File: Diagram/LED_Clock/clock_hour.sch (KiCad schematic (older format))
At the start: 28 parts, among them U4 MCP23017-E_SP

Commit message: updated
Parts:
- renumbered U4 to U1
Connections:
- net at R22.2: now also U1.4 (GPB3); no longer U1.21 (GPA0)
- net at R25.2: now also U1.1 (GPB0); no longer U1.24 (GPA3)
- net at R26.2: now also U1.28 (GPA7); no longer U1.25 (GPA4)
- net at R27.2: now also U1.27 (GPA6); no longer U1.26 (GPA5)
- net at R28.2: now also U1.26 (GPA5); no longer U1.27 (GPA6)
- net at U1.22 (GPA1): now also R32.2; no longer R23.2
- net at U1.23 (GPA2): now also R31.2; no longer R24.2
- net at R29.2: now also U1.25 (GPA4); no longer U1.28 (GPA7)
- net HGPB0: no longer names the net of R30.2
- net HGPB0: now also U1.24 (GPA3); no longer U1.1 (GPB0)
- net HGPB1: no longer names the net of U1.2 (GPB1)
- net HGPB1: now also R24.2; no longer R31.2
- net HGPB2: no longer names the net of U1.3 (GPB2)
- net HGPB2: now also R23.2; no longer R32.2
- net HGPB3: no longer names the net of R33.2
- net HGPB3: now also U1.21 (GPA0); no longer U1.4 (GPB3)
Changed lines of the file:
@@
 $EndComp
 $Comp
-L LED_Clock-rescue:MCP23017-E_SP-dk_Interface-I-O-Expanders U?
+L LED_Clock-rescue:MCP23017-E_SP-dk_Interface-I-O-Expanders U1
 U 1 1 5E559BAD
 P 2400 3200
-AR Path="/5E559BAD" Ref="U?"  Part="1"
+AR Path="/5E559BAD" Ref="U1"  Part="1"
 AR Path="/5E4DDBDE/5E559BAD" Ref="U4"  Part="1"
 F 0 "U4" H 2500 4550 60  0000 C CNN
@@
 	-1   0    0    1
 $EndComp
-Wire Wire Line
-	2700 3000 3950 3000
-Wire Wire Line
-	3950 3000 3950 2100
-Wire Wire Line
-	2700 2900 3850 2900
-Wire Wire Line
-	3850 2900 3850 1250
-Wire Wire Line
-	3850 1250 4400 1250
-Wire Wire Line
-	4400 1250 4400 2100
-Wire Wire Line
-	4400 2100 4500 2100
-Wire Wire Line
-	2700 2800 3800 2800
-Wire Wire Line
-	3800 2800 3800 1200
-Wire Wire Line
-	3800 1200 4950 1200
-Wire Wire Line
-	4950 1200 4950 2100
-Wire Wire Line
-	4950 2100 5050 2100
-Wire Wire Line
-	2700 2700 3750 2700
-Wire Wire Line
-	3750 2700 3750 1150
-Wire Wire Line
-	3750 1150 5500 1150
-Wire Wire Line
-	5500 1150 5500 2100
-Wire Wire Line
-	5500 2100 5600 2100
-Wire Wire Line
-	2700 2600 3700 2600
-Wire Wire Line
-	3700 2600 3700 1100
-Wire Wire Line
-	3700 1100 6100 1100
-Wire Wire Line
-	6100 1100 6100 2100
-Wire Wire Line
-	6100 2100 6150 2100
-Wire Wire Line
-	3650 2500 3650 1050
-Wire Wire Line
-	3650 1050 6600 1050
-Wire Wire Line
-	6600 1050 6600 2100
-Wire Wire Line
-	6600 2100 6700 2100
-Wire Wire Line
-	2700 2500 3650 2500
-Wire Wire Line
-	2700 2400 3600 2400
-Wire Wire Line
-	3600 2400 3600 1000
-Wire Wire Line
-	3600 1000 7100 1000
-Wire Wire Line
-	7100 1000 7100 2100
-Wire Wire Line
-	7100 2100 7250 2100
-Wire Wire Line
-	2700 2300 3550 2300
-Wire Wire Line
-	3550 2300 3550 950
-Wire Wire Line
-	3550 950  7700 950
-Wire Wire Line
-	7700 950  7700 2100
-Wire Wire Line
-	7700 2100 7800 2100
-Text GLabel 8350 2100 3    50   BiDi ~ 0
-HGPB0
-Text GLabel 2700 3800 2    50   BiDi ~ 0
-HGPB0
-Text GLabel 2700 3700 2    50   BiDi ~ 0
-HGPB1
-Text GLabel 8900 2100 3    50   BiDi ~ 0
-HGPB1
-Text GLabel 9450 2100 3    50   BiDi ~ 0
-HGPB2
-Text GLabel 2700 3600 2    50   BiDi ~ 0
-HGPB2
-Text GLabel 2700 3500 2    50   BiDi ~ 0
-HGPB3
-Text GLabel 10000 2100 3    50   BiDi ~ 0
-HGPB3
 Text HLabel 800  1250 0    50   Output ~ 0
 SDA
@@
 AR Path="/5E4DDAEE/5E8FB0A2" Ref="#PWR?"  Part="1"
 AR Path="/5E4DDBDE/5E8FB0A2" Ref="#PWR0101"  Part="1"
+AR Path="/5E8FB0A2" Ref="#PWR0101"  Part="1"
 F 0 "#PWR0101" H 3000 1550 50  0001 C CNN
 F 1 "GND" H 3005 1627 50  0000 C CNN
@@
 AR Path="/5E4DDAEE/5E8FB0AE" Ref="#PWR?"  Part="1"
 AR Path="/5E4DDBDE/5E8FB0AE" Ref="#PWR0103"  Part="1"
+AR Path="/5E8FB0AE" Ref="#PWR0103"  Part="1"
 F 0 "#PWR0103" H 3000 1650 50  0001 C CNN
 F 1 "GND" H 3005 1727 50  0000 C CNN
@@
 AR Path="/5E4DDAEE/5E8FB0B4" Ref="R?"  Part="1"
 AR Path="/5E4DDBDE/5E8FB0B4" Ref="R34"  Part="1"
+AR Path="/5E8FB0B4" Ref="R34"  Part="1"
 F 0 "R34" H 2920 1846 50  0000 L CNN
 F 1 "1k" H 2920 1755 50  0000 L CNN
@@
 AR Path="/5E4DDAEE/5E8FB0BA" Ref="R?"  Part="1"
 AR Path="/5E4DDBDE/5E8FB0BA" Ref="R35"  Part="1"
+AR Path="/5E8FB0BA" Ref="R35"  Part="1"
 F 0 "R35" H 2920 1946 50  0000 L CNN
 F 1 "1k" H 2920 1855 50  0000 L CNN
@@
 AR Path="/5E4DDAEE/5E8FB0C0" Ref="R?"  Part="1"
 AR Path="/5E4DDBDE/5E8FB0C0" Ref="R36"  Part="1"
+AR Path="/5E8FB0C0" Ref="R36"  Part="1"
 F 0 "R36" H 2920 2046 50  0000 L CNN
 F 1 "1k" H 2920 1955 50  0000 L CNN
@@
 	0    1    1    0
 $EndComp
+Wire Wire Line
+	2700 3500 3950 3500
+Wire Wire Line
+	3950 3500 3950 2100
+Wire Wire Line
+	2700 3600 4500 3600
+Wire Wire Line
+	4500 3600 4500 2100
+Wire Wire Line
+	2700 3700 5050 3700
+Wire Wire Line
+	5050 3700 5050 2100
+Wire Wire Line
+	2700 3800 5600 3800
+Wire Wire Line
+	5600 3800 5600 2100
+Wire Wire Line
+	2700 2300 6150 2300
+Wire Wire Line
+	6150 2300 6150 2100
+Wire Wire Line
+	2700 2400 6700 2400
+Wire Wire Line
+	6700 2400 6700 2100
+Wire Wire Line
+	2700 2500 7250 2500
+Wire Wire Line
+	7250 2500 7250 2100
+Wire Wire Line
+	2700 2600 7800 2600
+Wire Wire Line
+	7800 2600 7800 2100
+Wire Wire Line
+	2700 2700 8350 2700
+Wire Wire Line
+	8350 2700 8350 2100
+Wire Wire Line
+	2700 2800 8900 2800
+Wire Wire Line
+	8900 2800 8900 2100
+Wire Wire Line
+	2700 2900 9450 2900
+Wire Wire Line
+	9450 2900 9450 2100
+Wire Wire Line
+	2700 3000 10000 3000
+Wire Wire Line
+	10000 3000 10000 2100
 $EndSCHEMATC

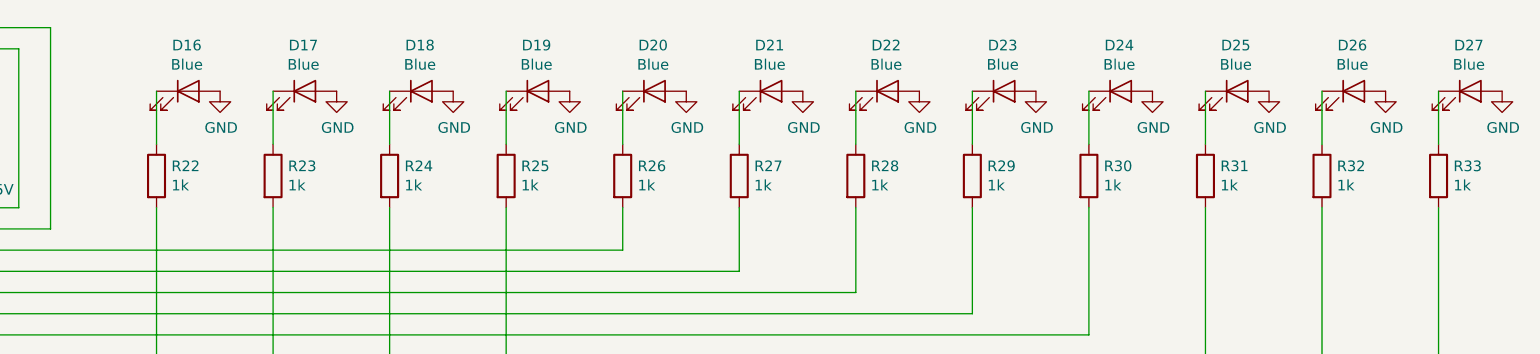
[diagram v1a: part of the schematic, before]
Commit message: Updated
led flipped the RTS symbol remade and JST4pin enlarged
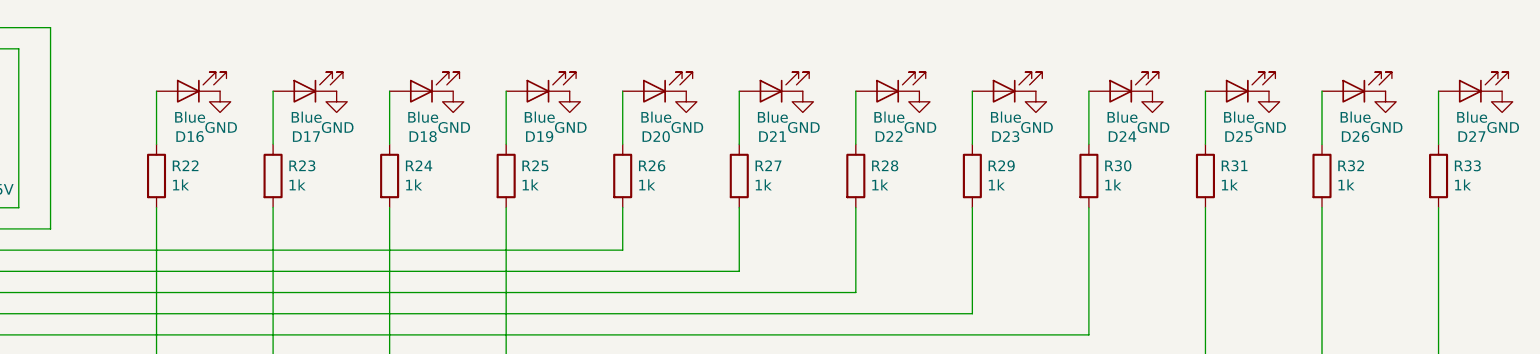
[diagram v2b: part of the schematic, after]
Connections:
- net GND: now also D16.1 (K), D17.1 (K), D18.1 (K), D19.1 (K), D20.1 (K), D21.1 (K), D22.1 (K), D23.1 (K), D24.1 (K), D25.1 (K), D26.1 (K), D27.1 (K); no longer D16.2 (A), D17.2 (A), D18.2 (A), D19.2 (A), D20.2 (A), D21.2 (A), D22.2 (A), D23.2 (A), D24.2 (A), D25.2 (A), D26.2 (A), D27.2 (A)
- net at R22.1: now also D16.2 (A); no longer D16.1 (K)
- net at R25.1: now also D19.2 (A); no longer D19.1 (K)
- net at R26.1: now also D20.2 (A); no longer D20.1 (K)
- net at R27.1: now also D21.2 (A); no longer D21.1 (K)
- net at R28.1: now also D22.2 (A); no longer D22.1 (K)
- net at R30.1: now also D24.2 (A); no longer D24.1 (K)
- net at R31.1: now also D25.2 (A); no longer D25.1 (K)
- net at R32.1: now also D26.2 (A); no longer D26.1 (K)
- net at R33.1: now also D27.2 (A); no longer D27.1 (K)
- net at R23.1: now also D17.2 (A); no longer D17.1 (K)
- net at R24.1: now also D18.2 (A); no longer D18.1 (K)
- net at R29.1: now also D23.2 (A); no longer D23.1 (K)
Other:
- moved on the sheet: D16, D17, D18, D19, D20, D21, D22, D23, D24, D25, D26, D27
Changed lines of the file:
@@
 F 3 "~" H 4100 1550 50  0001 C CNN
 	1    4100 1550
-	1    0    0    -1
+	-1   0    0    1
 $EndComp
 $Comp
@@
 F 3 "~" H 4650 1550 50  0001 C CNN
 	1    4650 1550
-	1    0    0    -1
+	-1   0    0    1
 $EndComp
 $Comp
@@
 F 3 "~" H 5200 1550 50  0001 C CNN
 	1    5200 1550
-	1    0    0    -1
+	-1   0    0    1
 $EndComp
 $Comp
@@
 F 3 "~" H 5750 1550 50  0001 C CNN
 	1    5750 1550
-	1    0    0    -1
+	-1   0    0    1
 $EndComp
 $Comp
@@
 F 3 "~" H 6300 1550 50  0001 C CNN
 	1    6300 1550
-	1    0    0    -1
+	-1   0    0    1
 $EndComp
 $Comp
@@
 F 3 "~" H 6850 1550 50  0001 C CNN
 	1    6850 1550
-	1    0    0    -1
+	-1   0    0    1
 $EndComp
 $Comp
@@
 F 3 "~" H 7400 1550 50  0001 C CNN
 	1    7400 1550
-	1    0    0    -1
+	-1   0    0    1
 $EndComp
 $Comp
@@
 F 3 "~" H 7950 1550 50  0001 C CNN
 	1    7950 1550
-	1    0    0    -1
+	-1   0    0    1
 $EndComp
 $Comp
@@
 F 3 "~" H 8500 1550 50  0001 C CNN
 	1    8500 1550
-	1    0    0    -1
+	-1   0    0    1
 $EndComp
 $Comp
@@
 F 3 "~" H 9050 1550 50  0001 C CNN
 	1    9050 1550
-	1    0    0    -1
+	-1   0    0    1
 $EndComp
 $Comp
@@
 F 3 "~" H 9600 1550 50  0001 C CNN
 	1    9600 1550
-	1    0    0    -1
+	-1   0    0    1
 $EndComp
 $Comp
@@
 F 3 "~" H 10150 1550 50  0001 C CNN
 	1    10150 1550
-	1    0    0    -1
-$EndComp
-$Comp
+	-1   0    0    1
+$EndComp
+$Comp
